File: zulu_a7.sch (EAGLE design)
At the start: 168 parts, among them J1 Pmod 2x6, Q1 12MHz 25ppm (FPGA + FT2232HQ), Q2 NMOS, Q3 MBT3904DW1T1, U1 XC7A35T-1CPG236C, U10 93LC46BT-I/SN, U2 FT2232HQ USB-UART/JTAG Bridge, U3 AS4C32M16SB-6TIN, U4 W25Q128JVSIQ, U8 LTC3569EUDC#TRPBF, X1 Molex 105017-0001 Micro-USB-B, X2 ZULU-CONN, X3 MICROSD_CONDM3AT-SF-PEJM5

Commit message: Split JP3 across the Pmod and give the 2.400 in board its parts back
The 2.400 in cut left J1 and JP3 with nowhere to stand. There is one piece of
board they can share: the Pmod is 15.24 mm of a 21.34 mm channel, and the 3.05
mm bands it leaves above and below itself are too shallow for anything that has
to be a rectangle. A 2x3 needs 4.42 mm of copper height. Two rows of three,
17.96 mm apart, need 1.52 each, and they fit with room over.

New package 2X03-SPLIT in pinhead, and a SPLIT device on PINHD-2X3 carrying the
same six connects, so JP3 keeps its pins, its nets and its symbol -- only the
footprint changed. Keepout is one band per row on purpose: a single rectangle
would cover the Pmod it straddles and read as a clash.

WHAT THIS COSTS. It is no longer a pluggable header -- nothing spans 17.96 mm
-- so these are six bare plated holes for flying leads. Not even 1x3 strips:
their bodies would come within 0.09 mm of the Pmod's shroud. The design note
already called JP3 archaic and the FT2232 does JTAG over USB on channel B, so
bare bring-up holes look like the right amount of ceremony for it.

Q1 lost the argument for the +x end: the JTAG rows are 6.60 wide against the
Pmod's 5.08 and take the x Q1 wanted. It went to the band between the FT2232
and the USB shell, 4.80 mm tall and unusable by anything bigger, and sits there
with half a millimetre either side. It stays on the front, which was always the
point -- no via to the FPGA's clock ball or the FT2232's OSCI -- and it is no
longer what caps the escape's fan-out ring.

The back-side decoupling field is pulled in from 18.00 to 13.90 wide because
those are through-holes and the barrels come out on that side. board_plan's
check cannot see it -- it skips pairs on opposite sides -- but make_board can:
hole_zones() reads the drills off whatever is placed, so the tiler moves the
capacitors rather than the header. C114, C115, C119 and C120 are back in the
line of fire and this is what handles them.

Measured, symmetri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
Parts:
- JP3: device pinhead:PINHD-2X3NOSILK -> pinhead:PINHD-2X3SPLIT
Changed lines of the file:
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@@
 <attribute name="MANF" value="Microchip"/>
 </part>
-<part name="JP3" library="pinhead" deviceset="PINHD-2X3" device="NOSILK" value="JTAG 2x3"/>
+<part name="JP3" library="pinhead" deviceset="PINHD-2X3" device="SPLIT" value="JTAG 2x3"/>
 <part name="R4" library="ctambe" deviceset="RES8" device="741X" value="100">
 <attribute name="DIGIKEY#" value="741X163101JPCT-ND"/>

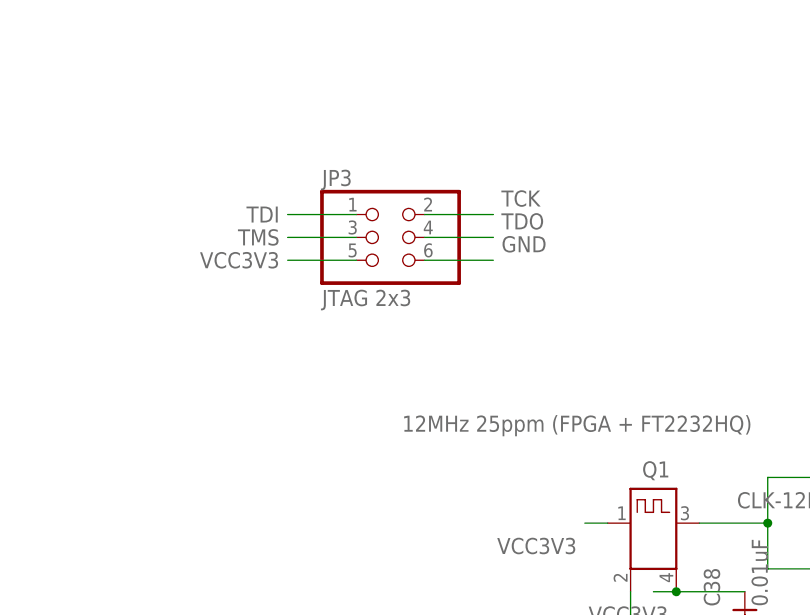
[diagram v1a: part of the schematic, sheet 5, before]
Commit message: Make the JTAG two 1x3 headers instead of one 2x3 telling a lie
The split footprint worked on the board and was wrong in the schematic. JP3 was
still drawn as a single 2x3 part, and a 2x3 is a thing you plug into. Nothing
plugs across 17.96 mm. Anyone reading the sheet would have believed a connector
that does not exist, and the only place the truth lived was a package
description two libraries away.

So the part follows the copper. JP3 is TCK/TMS/GND, JP4 is TDI/TDO/VCC3V3, both
PINHD-1X3 on the new 1X03-NOSILK footprint -- no silk, because a 2.54 mm body
would come within 0.09 mm of the Pmod's shroud. The six nets are unchanged: the
same TCK, TMS, GND, TDI, TDO and VCC3V3 land on the same six holes at the same
six coordinates. Only the part boundary moved.

Sheet 5 keeps JP3 where it was and puts JP4 15.24 mm below it, in a band that
had nothing in it. All six stubs now run left to a label, where the old 2x3
alternated left and right because its pins did.

Gone with it: PINHD-2X3, PINH2X3, and packages 2X03, 2X03-NOSILK and the
2X03-SPLIT from three commits ago -- 145 lines. pinhead is one deviceset, one
package, one symbol, all of them used.

TWO PARTS ALSO COUNT HONESTLY. 2X03-SPLIT's bounding box was 6.60 x 19.48, so
the area budget charged 129 mm2 for the whole region it straddled -- including
the Pmod standing inside it. Two 1x3s charge 20. Footprints drop 1652 -> 1543
mm2 and slack goes +77 -> +195 mm2, +3 % -> +8 %. The board did not change; the
arithmetic stopped double-counting.

validate.py 0 findings, placement check 15 blocks and 0 parked.

Co-Authored-By: Claude Opus 5 <noreply@anthropic.com>
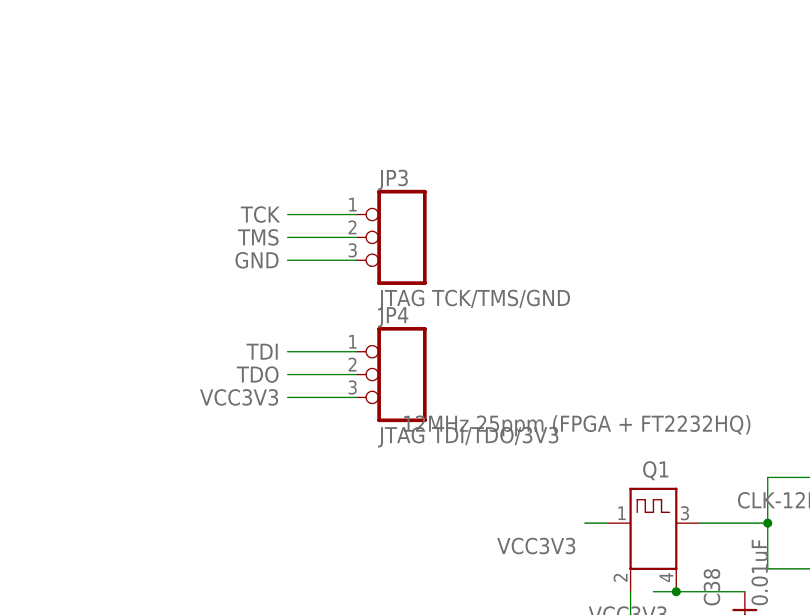
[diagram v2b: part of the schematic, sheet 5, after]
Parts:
- added JP4: JTAG TDI/TDO/3V3, pinhead:PINHD-1X3NOSILK
- JP3: value JTAG 2x3 -> JTAG TCK/TMS/GND; device pinhead:PINHD-2X3SPLIT -> pinhead:PINHD-1X3NOSILK
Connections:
- net GND: now also JP3.3; no longer JP3.6
- net TCK: now also JP3.1; no longer JP3.2
- net TDI: now also JP4.1; no longer JP3.1
- net TDO: now also JP4.2; no longer JP3.4
- net TMS: now also JP3.2; no longer JP3.3
- net VCC3V3: now also JP4.3; no longer JP3.5
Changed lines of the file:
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@@
 <attribute name="MANF" value="Microchip"/>
 </part>
-<part name="JP3" library="pinhead" deviceset="PINHD-2X3" device="SPLIT" value="JTAG 2x3"/>
+<part name="JP3" library="pinhead" deviceset="PINHD-1X3" device="NOSILK" value="JTAG TCK/TMS/GND"/>
+<part name="JP4" library="pinhead" deviceset="PINHD-1X3" device="NOSILK" value="JTAG TDI/TDO/3V3"/>
 <part name="R4" library="ctambe" deviceset="RES8" device="741X" value="100">
 <attribute name="DIGIKEY#" value="741X163101JPCT-ND"/>
@@
 </instance>
 <instance part="JP3" gate="A" x="46.99" y="72.39" smashed="yes">
-<attribute name="NAME" x="38.1" y="78.105" size="1.778" layer="95"/>
-<attribute name="VALUE" x="38.1" y="64.77" size="1.778" layer="96"/>
+<attribute name="NAME" x="44.45" y="78.105" size="1.778" layer="95"/>
+<attribute name="VALUE" x="44.45" y="64.77" size="1.778" layer="96"/>
+</instance>
+<instance part="JP4" gate="A" x="46.99" y="57.15" smashed="yes">
+<attribute name="NAME" x="44.45" y="62.865" size="1.778" layer="95"/>
+<attribute name="VALUE" x="44.45" y="49.53" size="1.778" layer="96"/>
 </instance>
 <instance part="R89" gate="G$1" x="154.94" y="241.3" smashed="yes" rot="MR90">
@@
 </segment>
 <segment>
-<wire x1="41.91" y1="69.85" x2="34.29" y2="69.85" width="0.1524" layer="91"/>
-<label x="33.4" y="70.74" size="1.778" layer="95" rot="R180"/>
-<pinref part="JP3" gate="A" pin="5"/>
+<wire x1="41.91" y1="54.61" x2="34.29" y2="54.61" width="0.1524" layer="91"/>
+<label x="33.4" y="55.5" size="1.778" layer="95" rot="R180"/>
+<pinref part="JP4" gate="A" pin="3"/>
 </segment>
 <segment>
@@
 </segment>
 <segment>
-<wire x1="49.53" y1="69.85" x2="57.15" y2="69.85" width="0.1524" layer="91"/>
-<label x="58.04" y="70.74" size="1.778" layer="95"/>
-<pinref part="JP3" gate="A" pin="6"/>
+<wire x1="41.91" y1="69.85" x2="34.29" y2="69.85" width="0.1524" layer="91"/>
+<label x="33.4" y="70.74" size="1.778" layer="95" rot="R180"/>
+<pinref part="JP3" gate="A" pin="3"/>
 </segment>
 <segment>
@@
 </segment>
 <segment>
-<wire x1="49.53" y1="74.93" x2="57.15" y2="74.93" width="0.1524" layer="91"/>
-<label x="58.04" y="75.82" size="1.778" layer="95"/>
-<pinref part="JP3" gate="A" pin="2"/>
+<wire x1="41.91" y1="74.93" x2="34.29" y2="74.93" width="0.1524" layer="91"/>
+<label x="33.4" y="75.82" size="1.778" layer="95" rot="R180"/>
+<pinref part="JP3" gate="A" pin="1"/>
 </segment>
 </net>
@@
 <wire x1="41.91" y1="72.39" x2="34.29" y2="72.39" width="0.1524" layer="91"/>
 <label x="33.4" y="73.28" size="1.778" layer="95" rot="R180"/>
-<pinref part="JP3" gate="A" pin="3"/>
+<pinref part="JP3" gate="A" pin="2"/>
 </segment>
 </net>
@@
 </segment>
 <segment>
-<wire x1="41.91" y1="74.93" x2="34.29" y2="74.93" width="0.1524" layer="91"/>
-<label x="33.4" y="75.82" size="1.778" layer="95" rot="R180"/>
-<pinref part="JP3" gate="A" pin="1"/>
+<wire x1="41.91" y1="59.69" x2="34.29" y2="59.69" width="0.1524" layer="91"/>
+<label x="33.4" y="60.58" size="1.778" layer="95" rot="R180"/>
+<pinref part="JP4" gate="A" pin="1"/>
 </segment>
 </net>
@@
 </segment>
 <segment>
-<wire x1="49.53" y1="72.39" x2="57.15" y2="72.39" width="0.1524" layer="91"/>
-<label x="58.04" y="73.28" size="1.778" layer="95"/>
-<pinref part="JP3" gate="A" pin="4"/>
+<wire x1="41.91" y1="57.15" x2="34.29" y2="57.15" width="0.1524" layer="91"/>
+<label x="33.4" y="58.04" size="1.778" layer="95" rot="R180"/>
+<pinref part="JP4" gate="A" pin="2"/>
 </segment>
 </net>
